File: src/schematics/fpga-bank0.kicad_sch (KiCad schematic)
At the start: 7 parts

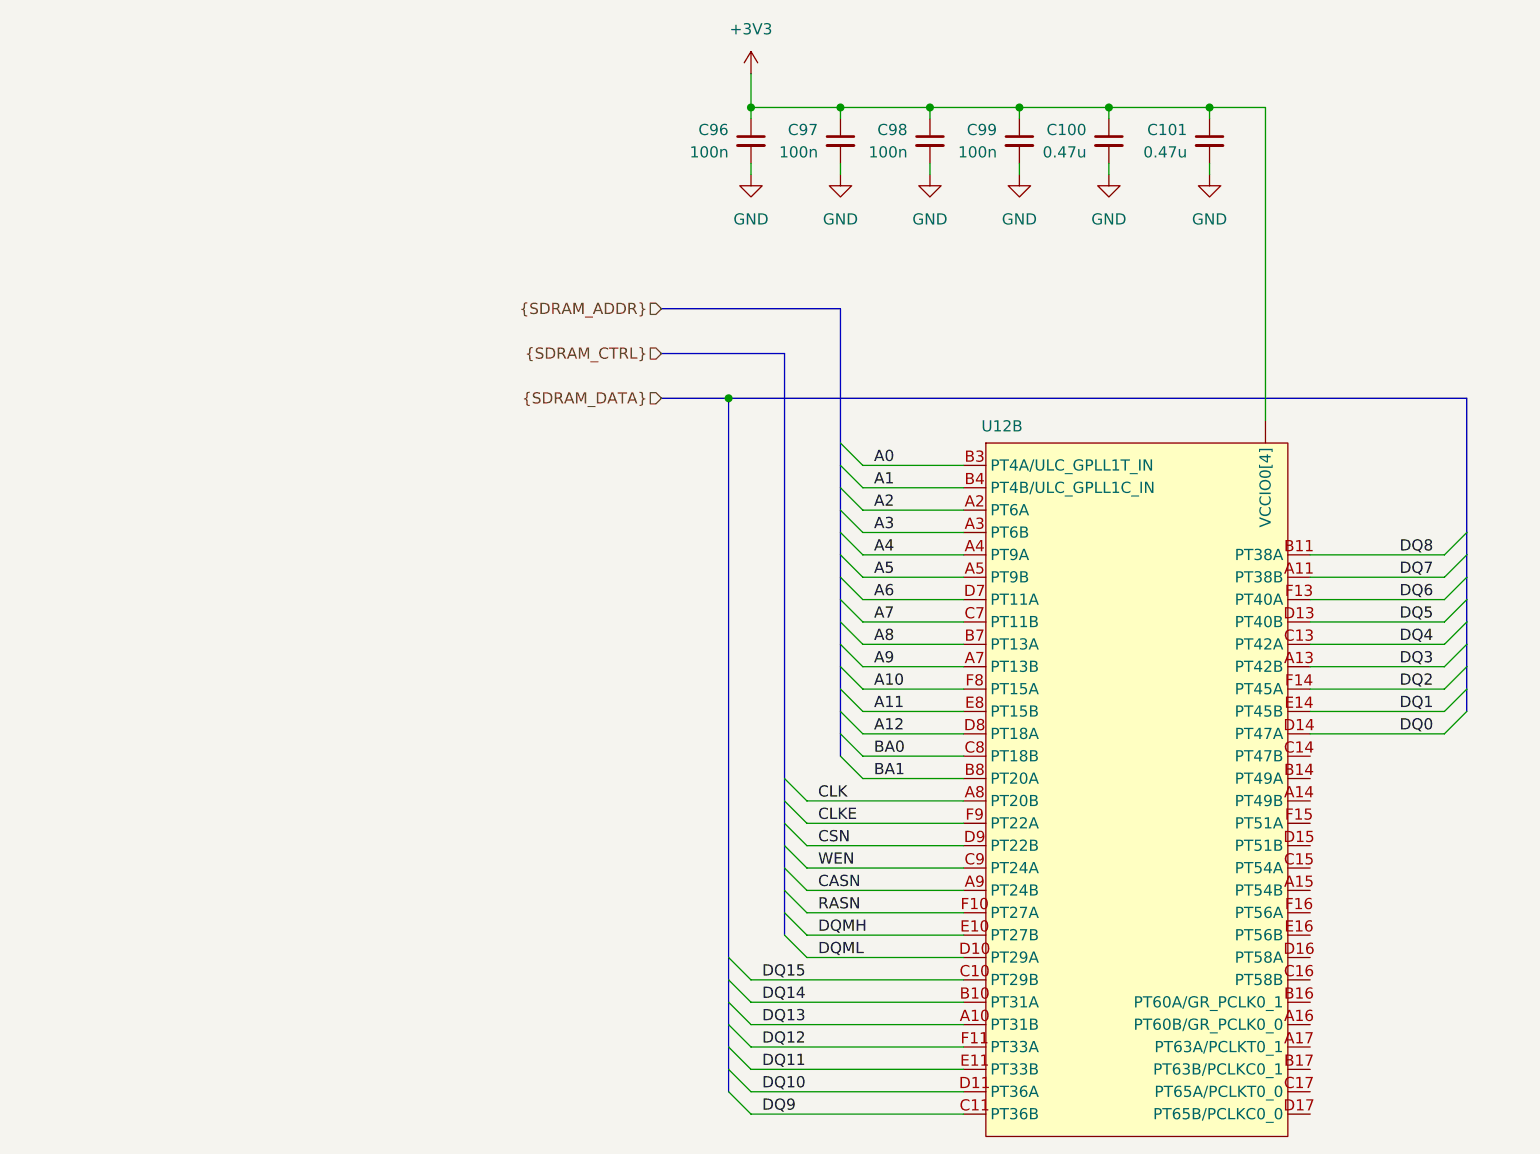
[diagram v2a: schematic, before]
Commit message: Adds the clock oscillator
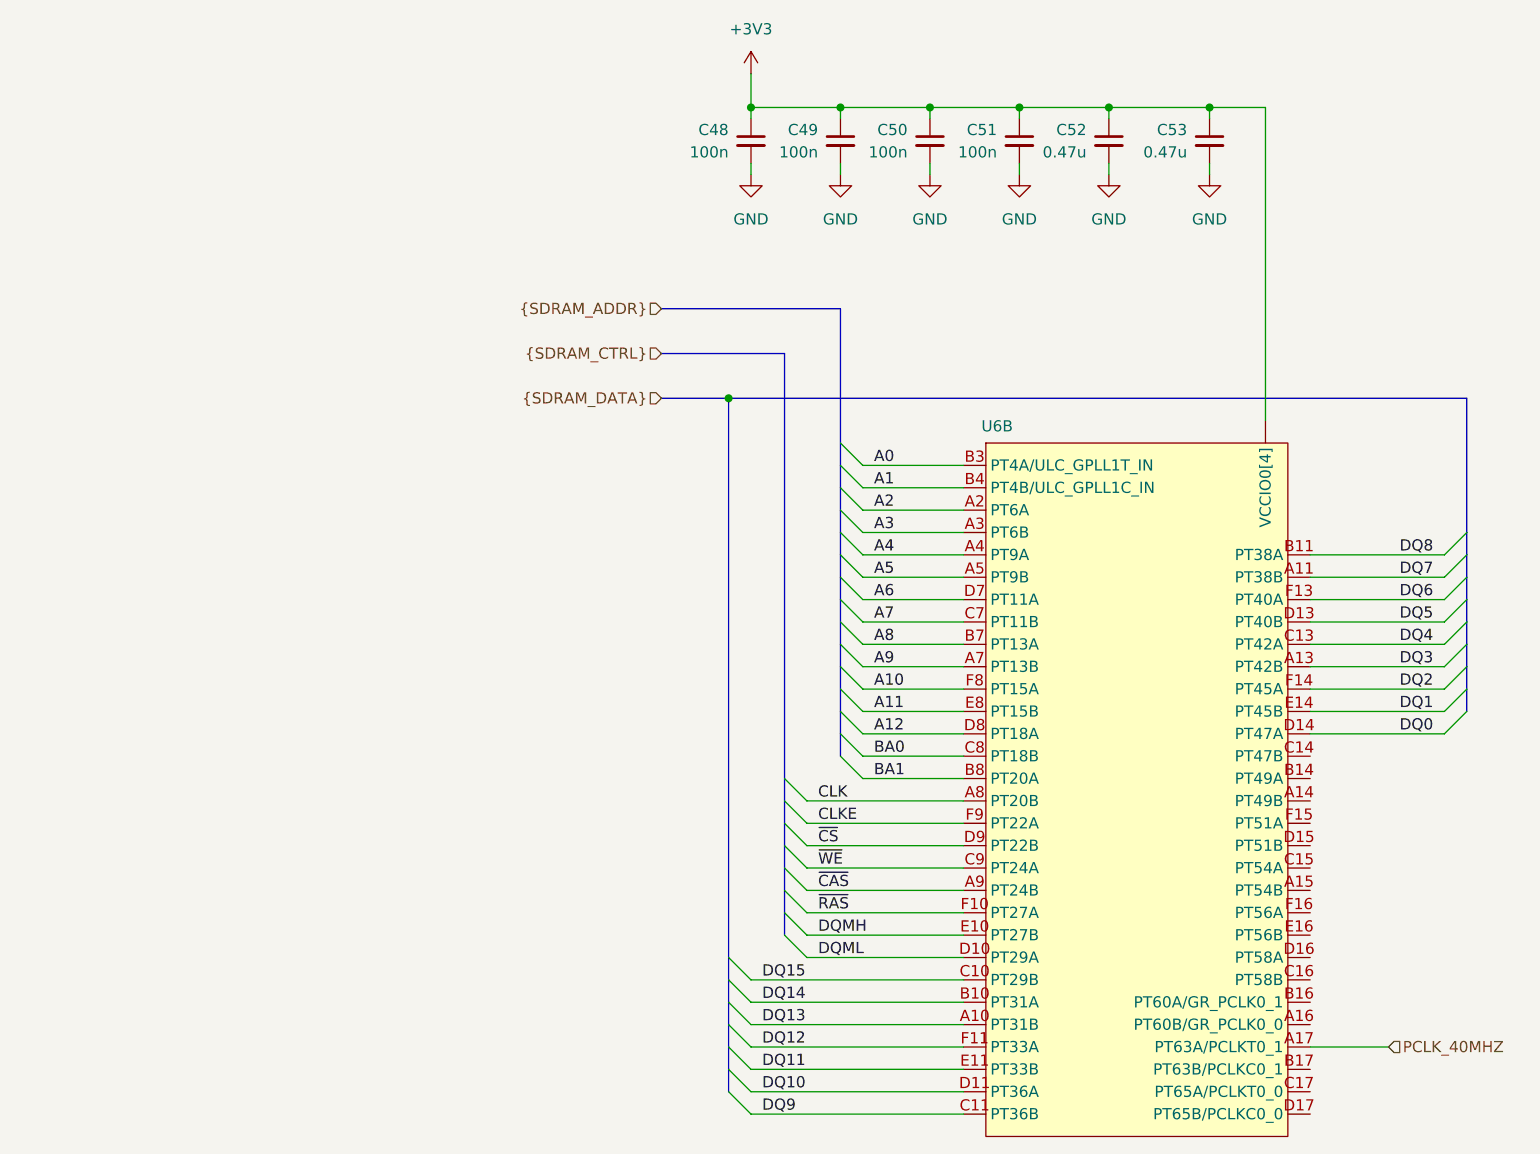
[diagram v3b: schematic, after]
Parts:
- renumbered C96 to C48, C97 to C49, C98 to C50, C99 to C51, C100 to C52, C101 to C53, U12 to U6
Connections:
- net PCLK_40MHZ: now reaches U6.A17 (PT63A/PCLKT0_1)
- net CASN renamed ~{CAS}
- net CSN renamed ~{CS}
- net RASN renamed ~{RAS}
- net WEN renamed ~{WE}
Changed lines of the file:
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@@
 		)
 	)
+	(wire
+		(pts
+			(xy 168.91 138.43) (xy 177.8 138.43)
+		)
+		(stroke
+			(width 0)
+			(type default)
+		)
+	)
 	(bus
 		(pts
@@
 		)
 	)
-	(label "RASN"
+	(label "~{RAS}"
 		(at 113.03 123.19 0)
 		(fields_autoplaced yes)
@@
 		)
 	)
-	(label "CASN"
+	(label "~{CAS}"
 		(at 113.03 120.65 0)
 		(fields_autoplaced yes)
@@
 		)
 	)
-	(label "CSN"
+	(label "~{CS}"
 		(at 113.03 115.57 0)
 		(fields_autoplaced yes)
@@
 		)
 	)
-	(label "WEN"
+	(label "~{WE}"
 		(at 113.03 118.11 0)
 		(fields_autoplaced yes)
@@
 		)
 	)
+	(hierarchical_label "PCLK_40MHZ"
+		(shape input)
+		(at 177.8 138.43 0)
+		(fields_autoplaced yes)
+		(effects
+			(font
+				(size 1.27 1.27)
+			)
+			(justify left)
+		)
+	)
 	(hierarchical_label "{SDRAM_CTRL}"
 		(shape input)
@@
 		(dnp no)
 		(fields_autoplaced yes)
-		(property "Reference" "C96"
+		(property "Reference" "C48"
 			(at 102.87 34.2962 0)
 			(effects
@@
 			(project "ecap5-bsom"
 				(path "/c5fd18a3-9aa0-4151-b6e0-94da3d606686/9ec64d27-698a-408d-bb9c-7e381193a80d/a27a4945-d3aa-4752-b726-05ef96a067ff"
-					(reference "C96")
+					(reference "C48")
 					(unit 1)
 				)
@@
 		(dnp no)
 		(fields_autoplaced yes)
-		(property "Reference" "#PWR0105"
+		(property "Reference" "#PWR026"
 			(at 105.41 45.72 0)
 			(effects
@@
 			(project "ecap5-bsom"
 				(path "/c5fd18a3-9aa0-4151-b6e0-94da3d606686/9ec64d27-698a-408d-bb9c-7e381193a80d/a27a4945-d3aa-4752-b726-05ef96a067ff"
-					(reference "#PWR0105")
+					(reference "#PWR026")
 					(unit 1)
 				)
@@
 		(dnp no)
 		(fields_autoplaced yes)
-		(property "Reference" "C99"
+		(property "Reference" "C51"
 			(at 133.35 34.2962 0)
 			(effects
@@
 			(project "ecap5-bsom"
 				(path "/c5fd18a3-9aa0-4151-b6e0-94da3d606686/9ec64d27-698a-408d-bb9c-7e381193a80d/a27a4945-d3aa-4752-b726-05ef96a067ff"
-					(reference "C99")
+					(reference "C51")
 					(unit 1)
 				)
@@
 		(dnp no)
 		(fields_autoplaced yes)
-		(property "Reference" "#PWR0108"
+		(property "Reference" "#PWR029"
 			(at 135.89 45.72 0)
 			(effects
@@
 			(project "ecap5-bsom"
 				(path "/c5fd18a3-9aa0-4151-b6e0-94da3d606686/9ec64d27-698a-408d-bb9c-7e381193a80d/a27a4945-d3aa-4752-b726-05ef96a067ff"
-					(reference "#PWR0108")
+					(reference "#PWR029")
 					(unit 1)
 				)
@@
 		(dnp no)
 		(fields_autoplaced yes)
-		(property "Reference" "#PWR097"
+		(property "Reference" "#PWR025"
 			(at 105.41 31.75 0)
 			(effects
@@
 			(project "ecap5-bsom"
 				(path "/c5fd18a3-9aa0-4151-b6e0-94da3d606686/9ec64d27-698a-408d-bb9c-7e381193a80d/a27a4945-d3aa-4752-b726-05ef96a067ff"
-					(reference "#PWR097")
+					(reference "#PWR025")
 					(unit 1)
 				)
@@
 		(dnp no)
 		(fields_autoplaced yes)
-		(property "Reference" "#PWR0107"
+		(property "Reference" "#PWR028"
 			(at 125.73 45.72 0)
 			(effects
@@
 			(project "ecap5-bsom"
 				(path "/c5fd18a3-9aa0-4151-b6e0-94da3d606686/9ec64d27-698a-408d-bb9c-7e381193a80d/a27a4945-d3aa-4752-b726-05ef96a067ff"
-					(reference "#PWR0107")
+					(reference "#PWR028")
 					(unit 1)
 				)
@@
 		(dnp no)
 		(fields_autoplaced yes)
-		(property "Reference" "C100"
+		(property "Reference" "C52"
 			(at 143.51 34.2962 0)
 			(effects
@@
 			(project "ecap5-bsom"
 				(path "/c5fd18a3-9aa0-4151-b6e0-94da3d606686/9ec64d27-698a-408d-bb9c-7e381193a80d/a27a4945-d3aa-4752-b726-05ef96a067ff"
-					(reference "C100")
+					(reference "C52")
 					(unit 1)
 				)
@@
 		(on_board yes)
 		(dnp no)
-		(property "Reference" "U12"
+		(property "Reference" "U6"
 			(at 131.572 67.9449 0)
 			(effects
@@
 			(project "ecap5-bsom"
 				(path "/c5fd18a3-9aa0-4151-b6e0-94da3d606686/9ec64d27-698a-408d-bb9c-7e381193a80d/a27a4945-d3aa-4752-b726-05ef96a067ff"
-					(reference "U12")
+					(reference "U6")
 					(unit 2)
 				)
@@
 		(dnp no)
 		(fields_autoplaced yes)
-		(property "Reference" "C98"
+		(property "Reference" "C50"
 			(at 123.19 34.2962 0)
 			(effects
@@
 			(project "ecap5-bsom"
 				(path "/c5fd18a3-9aa0-4151-b6e0-94da3d606686/9ec64d27-698a-408d-bb9c-7e381193a80d/a27a4945-d3aa-4752-b726-05ef96a067ff"
-					(reference "C98")
+					(reference "C50")
 					(unit 1)
 				)
@@
 		(dnp no)
 		(fields_autoplaced yes)
-		(property "Reference" "#PWR0109"
+		(property "Reference" "#PWR030"
 			(at 146.05 45.72 0)
 			(effects
@@
 			(project "ecap5-bsom"
 				(path "/c5fd18a3-9aa0-4151-b6e0-94da3d606686/9ec64d27-698a-408d-bb9c-7e381193a80d/a27a4945-d3aa-4752-b726-05ef96a067ff"
-					(reference "#PWR0109")
+					(reference "#PWR030")
 					(unit 1)
 				)
@@
 		(dnp no)
 		(fields_autoplaced yes)
-		(property "Reference" "#PWR0110"
+		(property "Reference" "#PWR031"
 			(at 157.48 45.72 0)
 			(effects
@@
 			(project "ecap5-bsom"
 				(path "/c5fd18a3-9aa0-4151-b6e0-94da3d606686/9ec64d27-698a-408d-bb9c-7e381193a80d/a27a4945-d3aa-4752-b726-05ef96a067ff"
-					(reference "#PWR0110")
+					(reference "#PWR031")
 					(unit 1)
 				)
@@
 		(dnp no)
 		(fields_autoplaced yes)
-		(property "Reference" "C101"
+		(property "Reference" "C53"
 			(at 154.94 34.2962 0)
 			(effects
@@
 			(project "ecap5-bsom"
 				(path "/c5fd18a3-9aa0-4151-b6e0-94da3d606686/9ec64d27-698a-408d-bb9c-7e381193a80d/a27a4945-d3aa-4752-b726-05ef96a067ff"
-					(reference "C101")
+					(reference "C53")
 					(unit 1)
 				)
@@
 		(dnp no)
 		(fields_autoplaced yes)
-		(property "Reference" "C97"
+		(property "Reference" "C49"
 			(at 113.03 34.2962 0)
 			(effects
@@
 			(project "ecap5-bsom"
 				(path "/c5fd18a3-9aa0-4151-b6e0-94da3d606686/9ec64d27-698a-408d-bb9c-7e381193a80d/a27a4945-d3aa-4752-b726-05ef96a067ff"
-					(reference "C97")
+					(reference "C49")
 					(unit 1)
 				)
@@
 		(dnp no)
 		(fields_autoplaced yes)
-		(property "Reference" "#PWR0106"
+		(property "Reference" "#PWR027"
 			(at 115.57 45.72 0)
 			(effects
@@
 			(project "ecap5-bsom"
 				(path "/c5fd18a3-9aa0-4151-b6e0-94da3d606686/9ec64d27-698a-408d-bb9c-7e381193a80d/a27a4945-d3aa-4752-b726-05ef96a067ff"
-					(reference "#PWR0106")
+					(reference "#PWR027")
 					(unit 1)
 				)

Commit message: Adds bus aliases
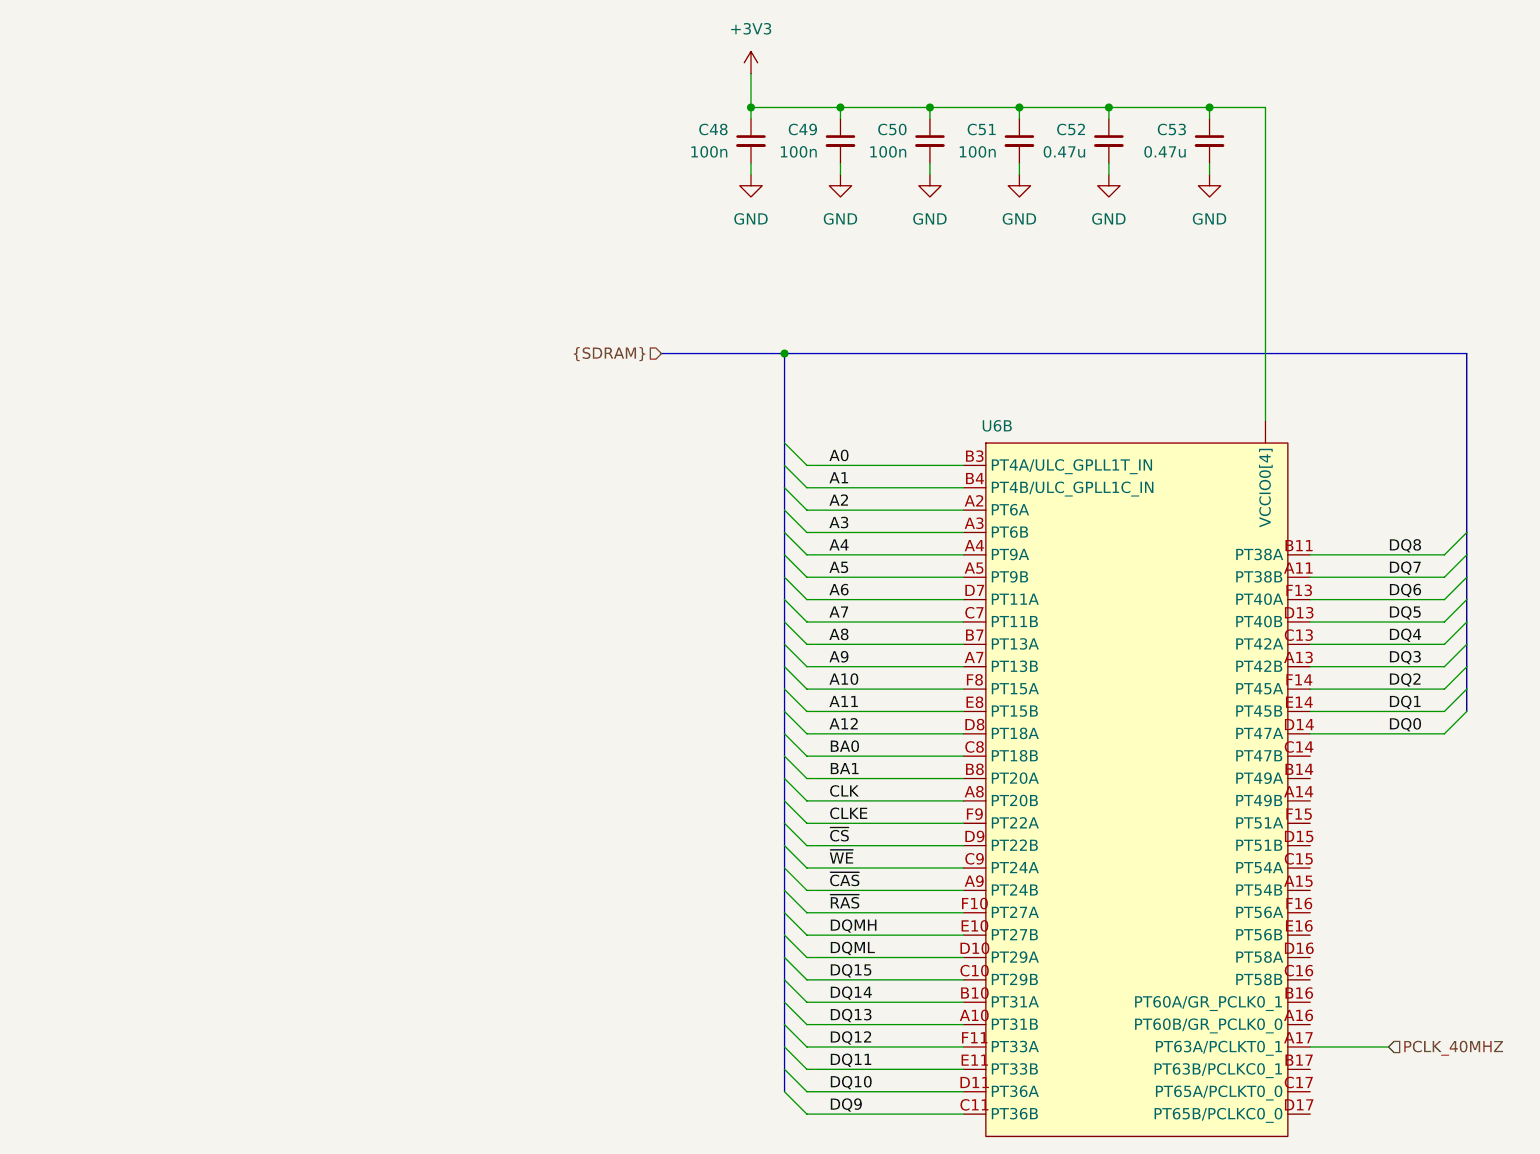
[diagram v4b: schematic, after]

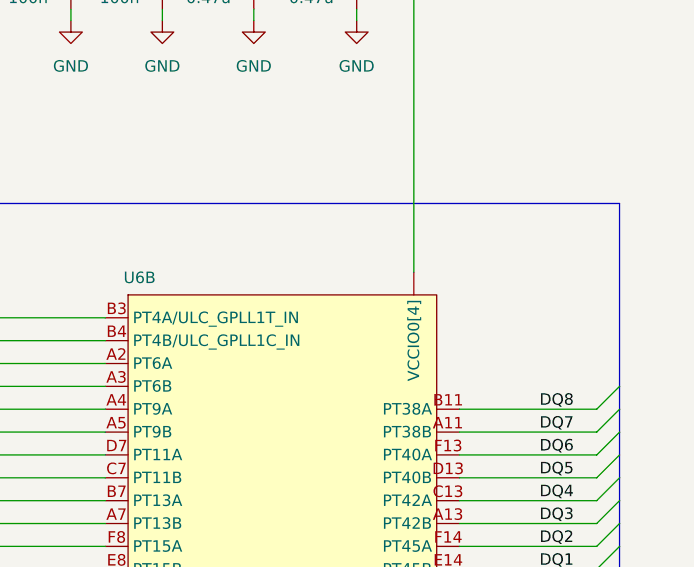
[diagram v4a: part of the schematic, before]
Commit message: Fix some ERC issues
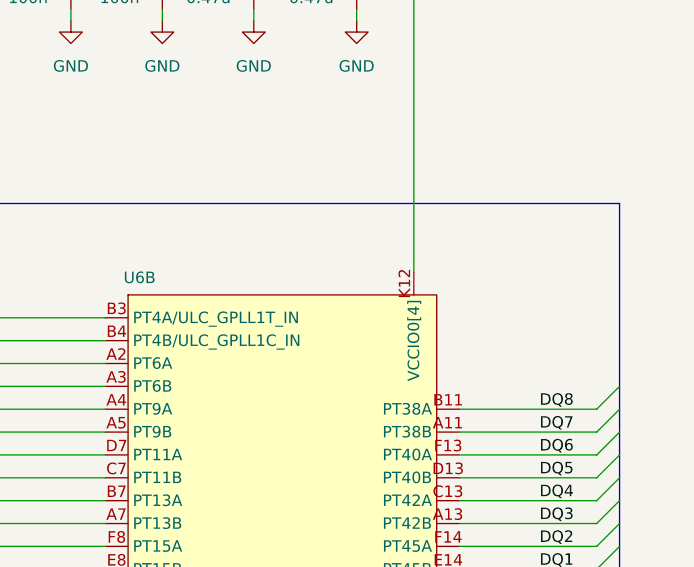
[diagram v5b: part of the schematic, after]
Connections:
- net +3V3: no longer U6. (VCCIO0[4])
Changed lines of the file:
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@@
 		(pin "Y31"
 		)
-		(pin ""
-		)
 		(pin "A10"
 		)
@@
 		(pin "Y32"
 		)
-		(pin ""
-		)
 		(pin "AB23"
 		)
@@
 		(pin "K16"
 		)
-		(pin ""
-		)
 		(pin "A18"
 		)
@@
 		(pin "K21"
 		)
-		(pin ""
-		)
 		(pin "B32"
 		)
@@
 		(pin "T23"
 		)
-		(pin ""
-		)
 		(pin "AA23"
 		)
@@
 		(pin "AM31"
 		)
-		(pin ""
-		)
 		(pin "AA10"
 		)
@@
 		(pin "Y7"
 		)
-		(pin ""
-		)
 		(pin "B1"
 		)
@@
 		(pin "T10"
 		)
-		(pin ""
-		)
 		(pin "AB10"
 		)
@@
 		(pin "M14"
 		)
-		(pin ""
-		)
 		(pin "AH12"
 		)
@@
 		(pin "V19"
 		)
-		(pin ""
-		)
 		(pin "AC11"
 		)
@@
 		(pin "AA11"
 		)
-		(pin ""
-		)
 		(instances

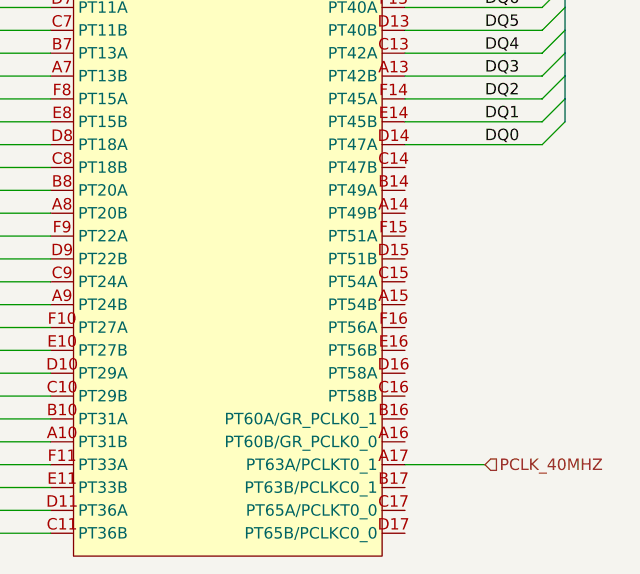
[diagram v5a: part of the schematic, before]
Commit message: Fixes bus aliases
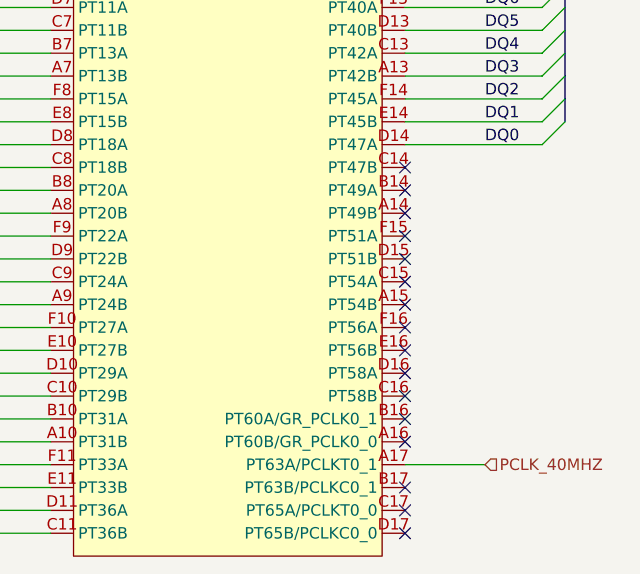
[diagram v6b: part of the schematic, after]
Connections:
- no-connect marks 0 -> 16
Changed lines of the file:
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@@
 		(color 0 0 0 0)
+	)
+	(no_connect
+		(at 168.91 115.57)
+	)
+	(no_connect
+		(at 168.91 130.81)
+	)
+	(no_connect
+		(at 168.91 105.41)
+	)
+	(no_connect
+		(at 168.91 140.97)
+	)
+	(no_connect
+		(at 168.91 118.11)
+	)
+	(no_connect
+		(at 168.91 146.05)
+	)
+	(no_connect
+		(at 168.91 133.35)
+	)
+	(no_connect
+		(at 168.91 143.51)
+	)
+	(no_connect
+		(at 168.91 135.89)
+	)
+	(no_connect
+		(at 168.91 128.27)
+	)
+	(no_connect
+		(at 168.91 123.19)
+	)
+	(no_connect
+		(at 168.91 107.95)
+	)
+	(no_connect
+		(at 168.91 113.03)
+	)
+	(no_connect
+		(at 168.91 120.65)
+	)
+	(no_connect
+		(at 168.91 110.49)
+	)
+	(no_connect
+		(at 168.91 125.73)
 	)
 	(bus_entry
@@
 		(pin "AB32"
 		)
-		(pin "AB32"
+		(pin "AB31"
 		)
 		(pin "AC26"
